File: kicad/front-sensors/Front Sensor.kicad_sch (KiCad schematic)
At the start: 0 parts

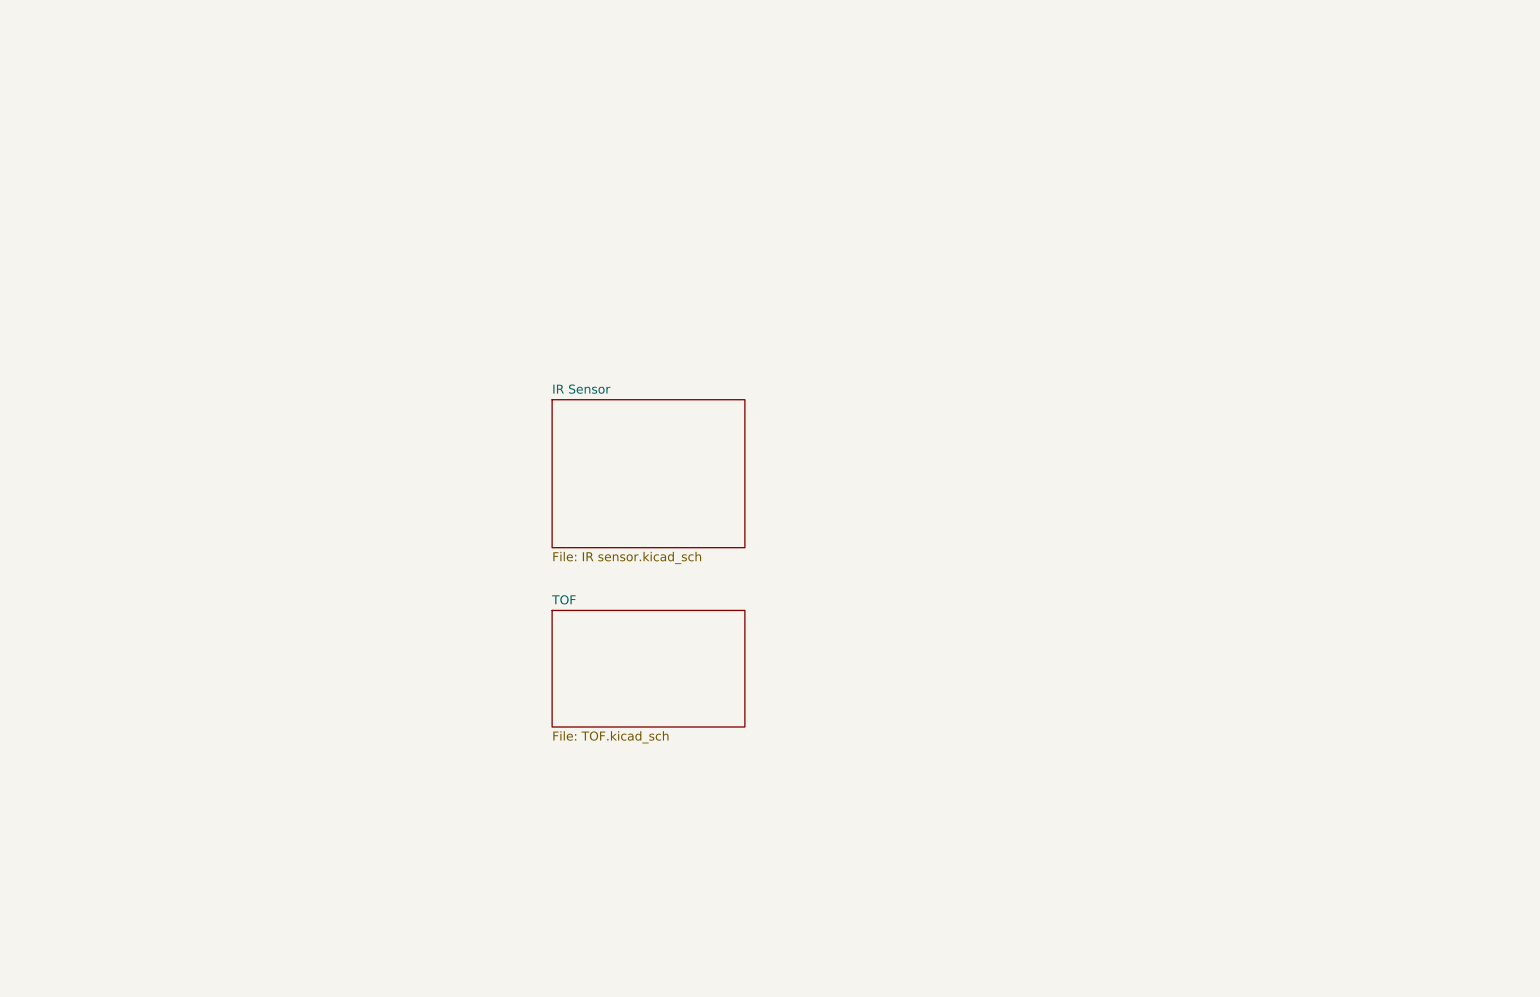
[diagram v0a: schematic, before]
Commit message: Front sensors rev 2: IR receivers onto main-phone, ToF board x2 on JST SH
- main-phone FRONT SENSORS: IR-F1/IR-F2 connectors replaced by two
  side-looking IRM-V838M3-C receivers on the board (U7501 left, U7502
  right) with 100R + 10uF filters; IRM-H638T is top-looking
- VL-L1/VL-R1: ZX-SH1.0-7PWT (JST SH compatible), same pinout
- kicad/front-sensors: one VL53L7 breakout fitted twice, refs 83xx, no
  pull-ups (main board has them), RSVD6 47k, ferrite to AVDD; the sensor
  is hand-placed (not in the JLC BOM/CPL); uses the shared ../main libs
- shared JLCImport: VL53L7, BLM18PG121SN1D, IRM-V838M3-C, ZX-SH1_0-7PWT
- docs: SPEC, READMEs, new front-sensors README

Co-Authored-By: Claude Opus 5.5 (1M context) <noreply@anthropic.com>
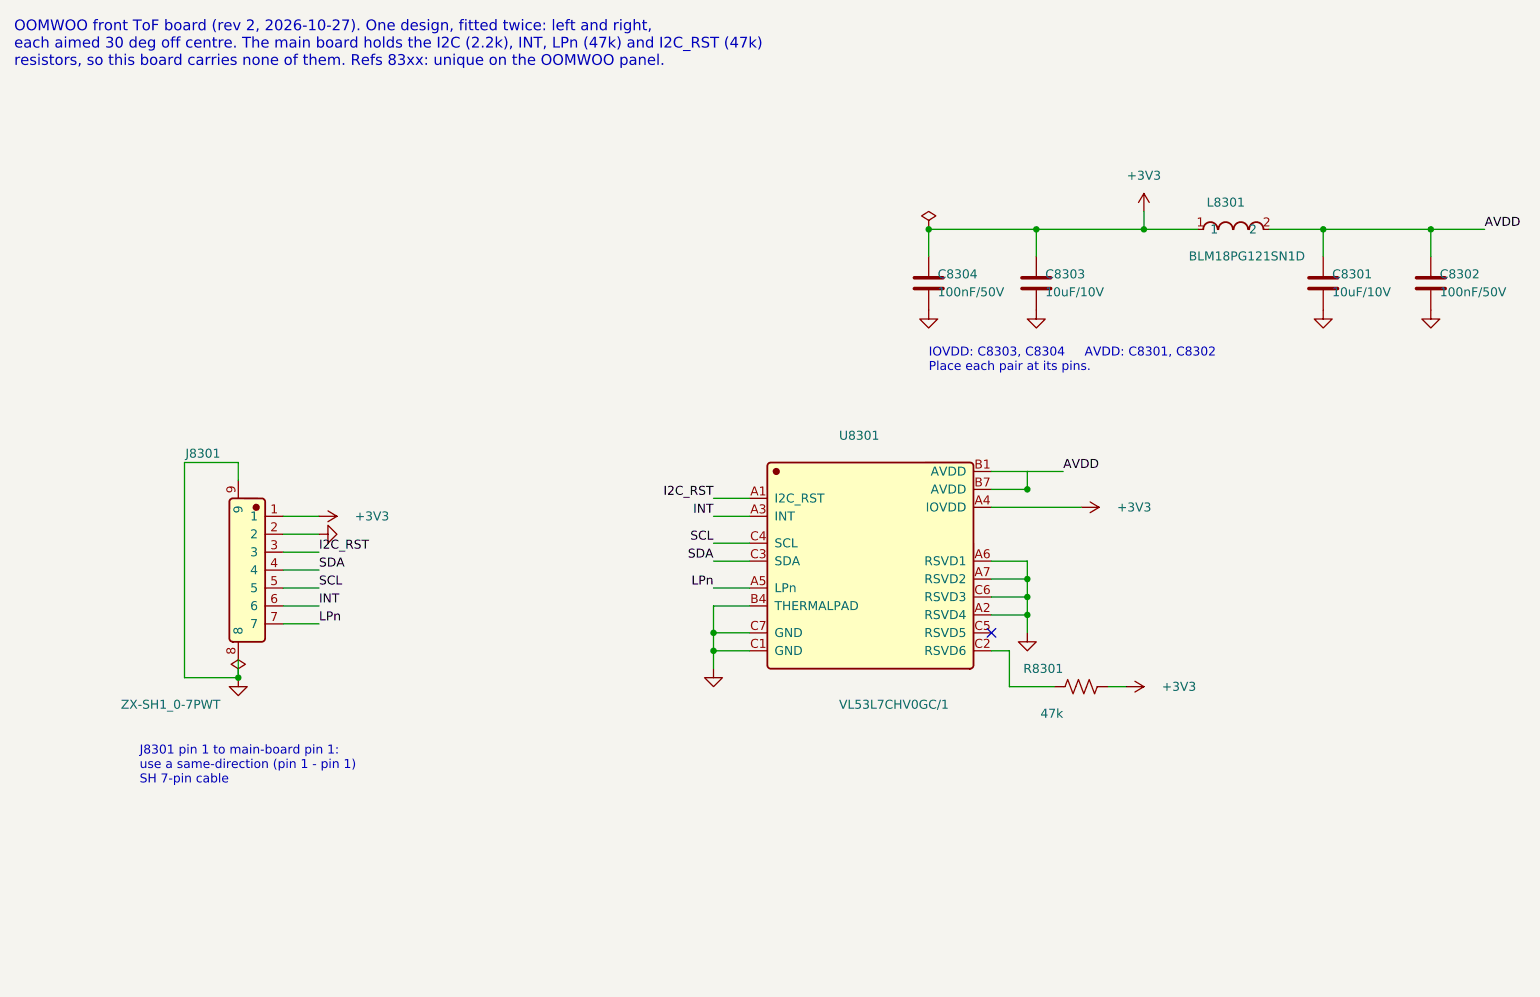
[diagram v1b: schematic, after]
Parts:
- added C8301, C8303: 10uF/10V, Capacitor_SMD:C_0603_1608Metric, symbol Device:C
- added C8302, C8304: 100nF/50V, Capacitor_SMD:C_0603_1608Metric, symbol Device:C
- added J8301: ZX-SH1_0-7PWT, JLCImport:ZX-SH1_0-7PWT, symbol JLCImport:ZX-SH1_0-7PWT
- added L8301: BLM18PG121SN1D, JLCImport:BLM18PG121SN1D, symbol JLCImport:BLM18PG121SN1D
- added R8301: 47k, Resistor_SMD:R_0603_1608Metric, symbol Device:R_US
- added U8301: VL53L7CHV0GC/1, JLCImport:VL53L7CHV0GC_1, symbol JLCImport:VL53L7CHV0GC_1
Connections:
- new net: R8301.1, U8301.C2 (RSVD6)
- new net +3V3: C8303.1, C8304.1, J8301.1, L8301.1, R8301.2, U8301.A4 (IOVDD)
- new net AVDD: C8301.1, C8302.1, L8301.2, U8301.B1 (AVDD), U8301.B7 (AVDD)
- new net GND: C8301.2, C8302.2, C8303.2, C8304.2, J8301.2, J8301.8, J8301.9, U8301.A2 (RSVD4), U8301.A6 (RSVD1), U8301.A7 (RSVD2), U8301.B4 (THERMALPAD), U8301.C1 (GND), U8301.C6 (RSVD3), U8301.C7 (GND)
- new net I2C_RST: J8301.3, U8301.A1 (I2C_RST)
- new net INT: J8301.6, U8301.A3 (INT)
- new net LPn: J8301.7, U8301.A5 (LPn)
- new net SCL: J8301.5, U8301.C4 (SCL)
- new net SDA: J8301.4, U8301.C3 (SDA)
- no-connect marks 0 -> 1
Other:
- removed sheet IR Sensor
- removed sheet TOF
- note added: "IOVDD: C8303, C8304 AVDD: C8301, C8302 Place each pair at its pins."
- note added: "J8301 pin 1 to main-board pin 1: use a same-direction (pin 1 - pin 1) SH 7-pin cable"
- note added: "OOMWOO front ToF board (rev 2, 2026-10-27). One design, fitted twice: left and right, each aimed 30 deg off centre. The main board holds the I2C (2.2k), INT, LPn (47k) and I2C_RST (47k) resistors, so this board carries none of them. Refs 83xx: unique on the OOMWOO panel."
- company: (none) -> OOMWOO front sensors
- title: (none) -> Front ToF sensor board (fit 2x)

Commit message: Side sensor board rev 2 (VL53L0X + IRM-H638T, JST SH); mounting holes on dock and sensor boards
- kicad/side-sensors: VL53L0X (C91199) replaces the NRND VL6180 and its 2.8 V LDO;
  top-looking IRM-H638T replaces the TSOP38238; ZX-SH1.0-7PWT connector, same pinout;
  10k XSHUT/GPIO1 pull-ups, no local I2C pull-ups; refs 84xx; libs from ../main
- main-phone SIDE-R1: ZX-ZH1.5-7PWT -> ZX-SH1.0-7PWT
- mounting holes: dock 4x M3 (H8201-H8204), ToF board 2x M2 (H8301/H8302),
  side board 2x M2 (H8401/H8402)
- JLCImport: VL53L0CXV0DH_1 symbol, footprint, 3D model
- docs: side board README, SPEC, READMEs; IRM-H638T pinout confirmed

Co-Authored-By: Claude Opus 5.5 (1M context) <noreply@anthropic.com>
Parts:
- added H8301, H8302: M2, MountingHole:MountingHole_2.2mm_M2_Pad, symbol Mechanical:MountingHole_Pad
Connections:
- net GND: now also H8301.1, H8302.1
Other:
- note added: "Mounting: 2x M2 (pads to GND)"
